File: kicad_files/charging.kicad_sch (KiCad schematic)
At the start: 2 parts, among them U2 BQ24650, U7 TL431DBZ

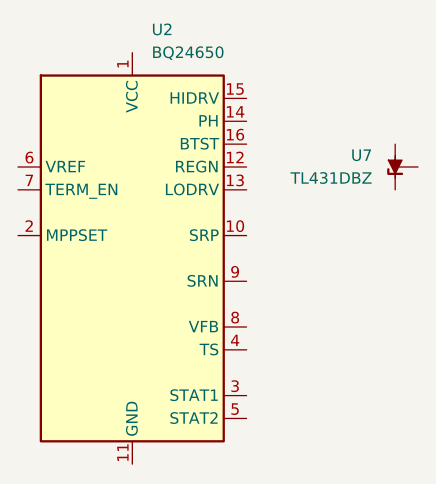
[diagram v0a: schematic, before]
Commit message: Remove power supply and add charging schematic instead
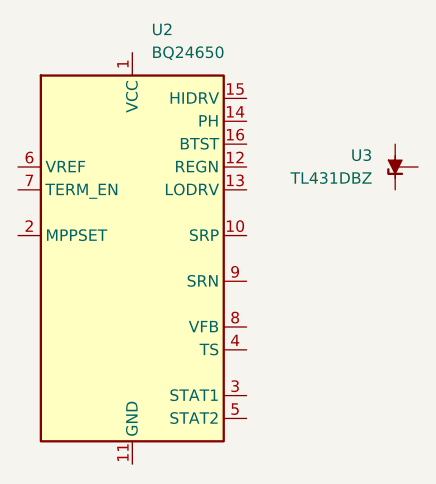
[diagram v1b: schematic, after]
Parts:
- renumbered U7 to U3
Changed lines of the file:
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@@
 		(dnp no)
 		(fields_autoplaced yes)
-		(property "Reference" "U7"
+		(property "Reference" "U3"
 			(at 157.48 52.0699 90)
 			(show_name no)
@@
 		(instances
 			(project "sodiumBMS"
-				(path "/fcdd2084-f4ec-4b1b-b9ac-497c327c0303/849bf9de-8a71-45bf-974a-6cae7b9f0dac"
-					(reference "U7")
+				(path "/fcdd2084-f4ec-4b1b-b9ac-497c327c0303/1b7ae7cb-6ce5-4b44-9aa9-df27edf3853f"
+					(reference "U3")
 					(unit 1)
 				)
@@
 		(instances
 			(project "sodiumBMS"
-				(path "/fcdd2084-f4ec-4b1b-b9ac-497c327c0303/849bf9de-8a71-45bf-974a-6cae7b9f0dac"
+				(path "/fcdd2084-f4ec-4b1b-b9ac-497c327c0303/1b7ae7cb-6ce5-4b44-9aa9-df27edf3853f"
 					(reference "U2")
 					(unit 1)
